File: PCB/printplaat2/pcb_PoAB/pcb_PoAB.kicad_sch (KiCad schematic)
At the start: 30 parts, among them J1 Conn_01x02_Female, J2 INA219_1, J3 INA219_2, J4 INA219_3, J5 INA219_4, J6 lamp1, J7 lamp2, J8 lamp3, U1 L7805CV, U2 AQY211EHAZ, U3 AQY211EHAZ, U4 AQY211EHAZ, U5 ACS712ELCTR-05B-T, U6 ACS712ELCTR-05B-T, U7 ACS712ELCTR-05B-T, U8 ACS712ELCTR-05B-T, U9 ARDUINO_MKR_WAN_1310

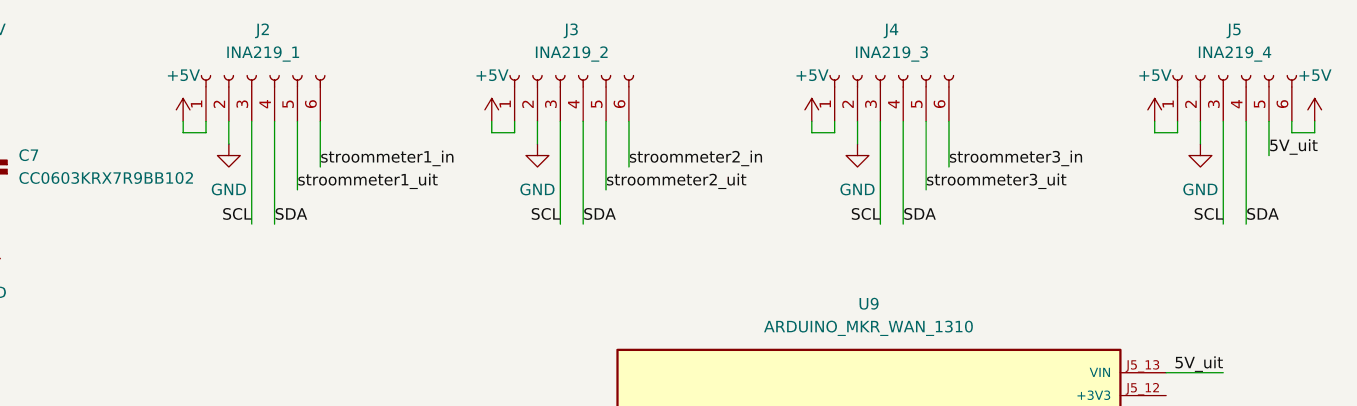
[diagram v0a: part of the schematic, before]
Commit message: pcb lichsensor toegevoegd
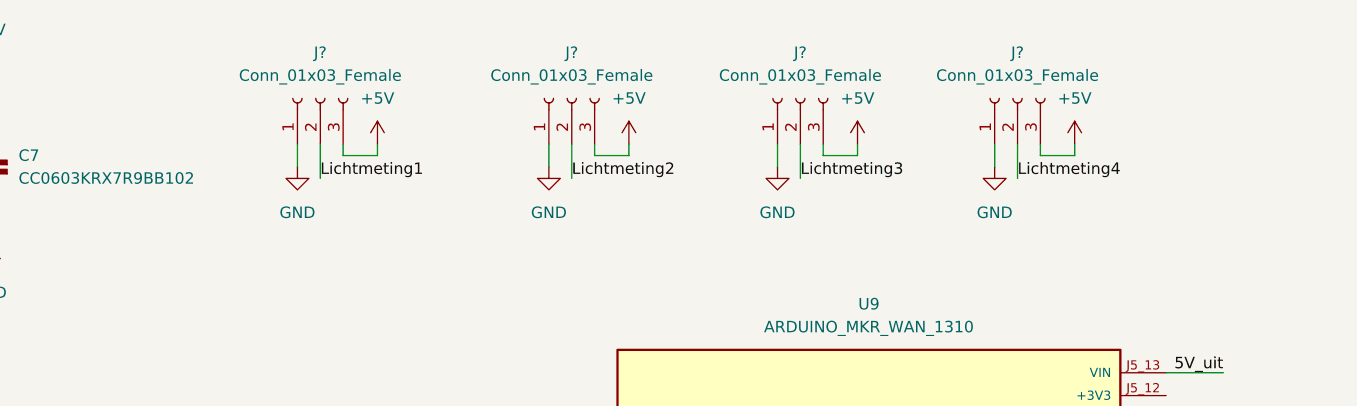
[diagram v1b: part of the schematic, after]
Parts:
- removed J2: INA219_1, symbol Connector:Conn_01x06_Female
- removed J3: INA219_2, symbol Connector:Conn_01x06_Female
- removed J4: INA219_3, symbol Connector:Conn_01x06_Female
- removed J5: INA219_4, symbol Connector:Conn_01x06_Female
- added J? (x4): Conn_01x03_Female, symbol Connector:Conn_01x03_Female
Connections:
- net +5V: now also J?.3 (Pin_3), J?.3 (Pin_3), J?.3 (Pin_3), J?.3 (Pin_3)
- net GND: now also J?.1 (Pin_1), J?.1 (Pin_1), J?.1 (Pin_1), J?.1 (Pin_1)
- new net Lichtmeting1: J?.2 (Pin_2)
- new net Lichtmeting2: J?.2 (Pin_2)
- new net Lichtmeting3: J?.2 (Pin_2)
- new net Lichtmeting4: J?.2 (Pin_2)

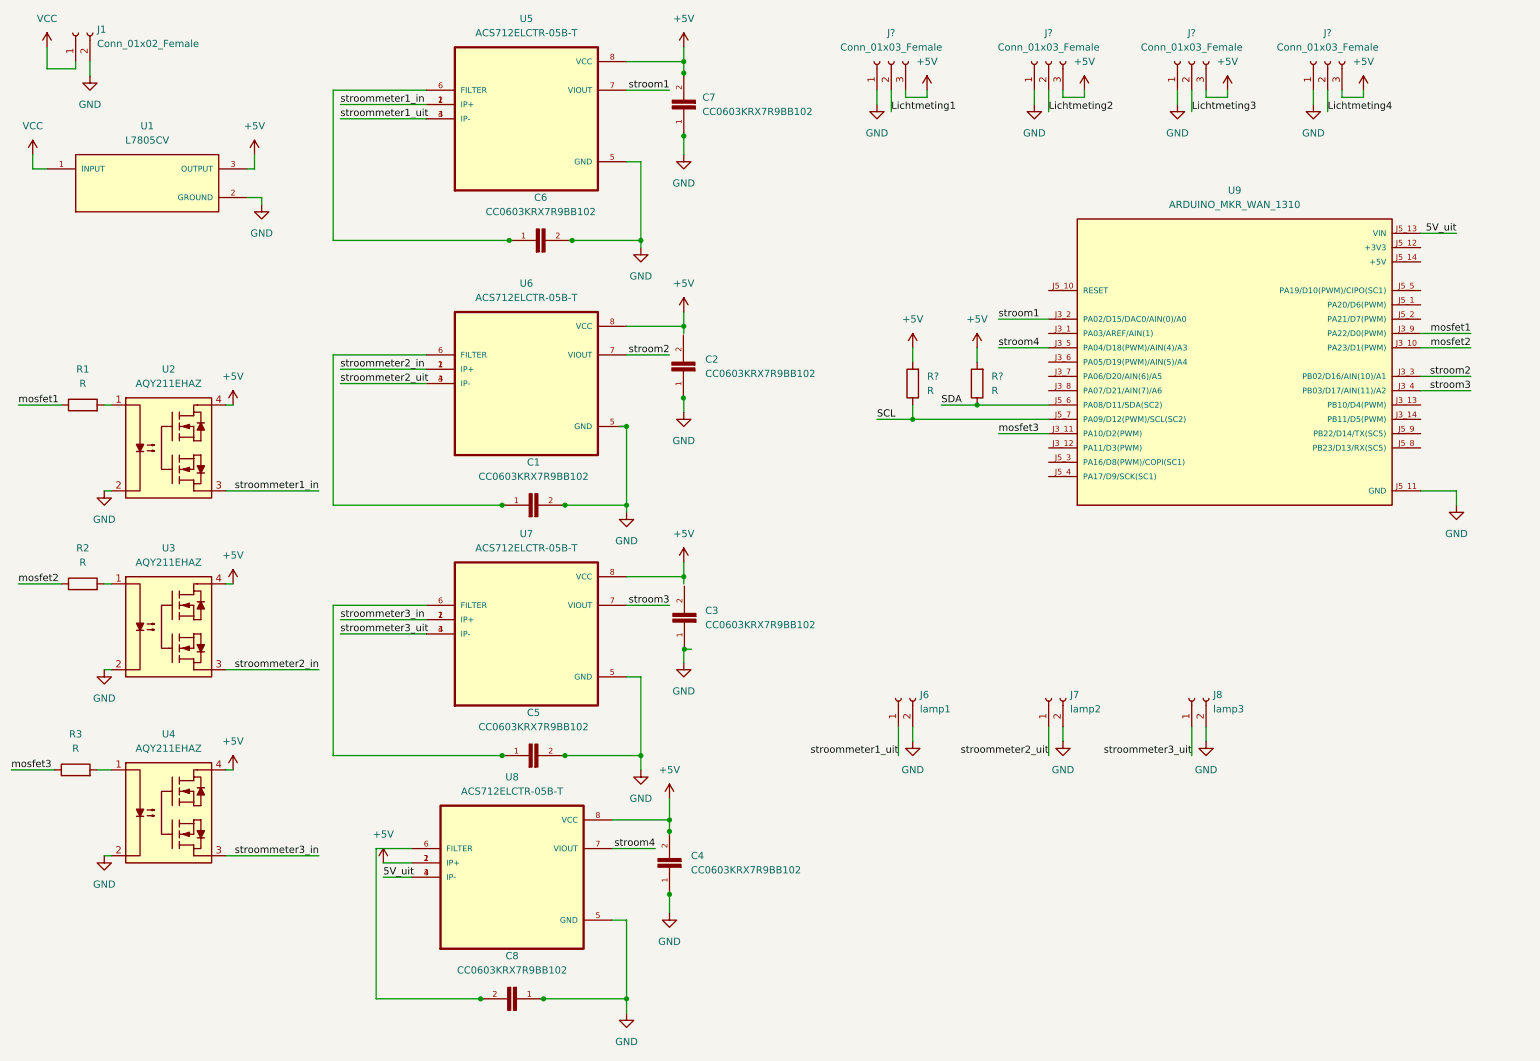
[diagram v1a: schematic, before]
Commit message: lichtmetingen en voltage metingen toegevoegd
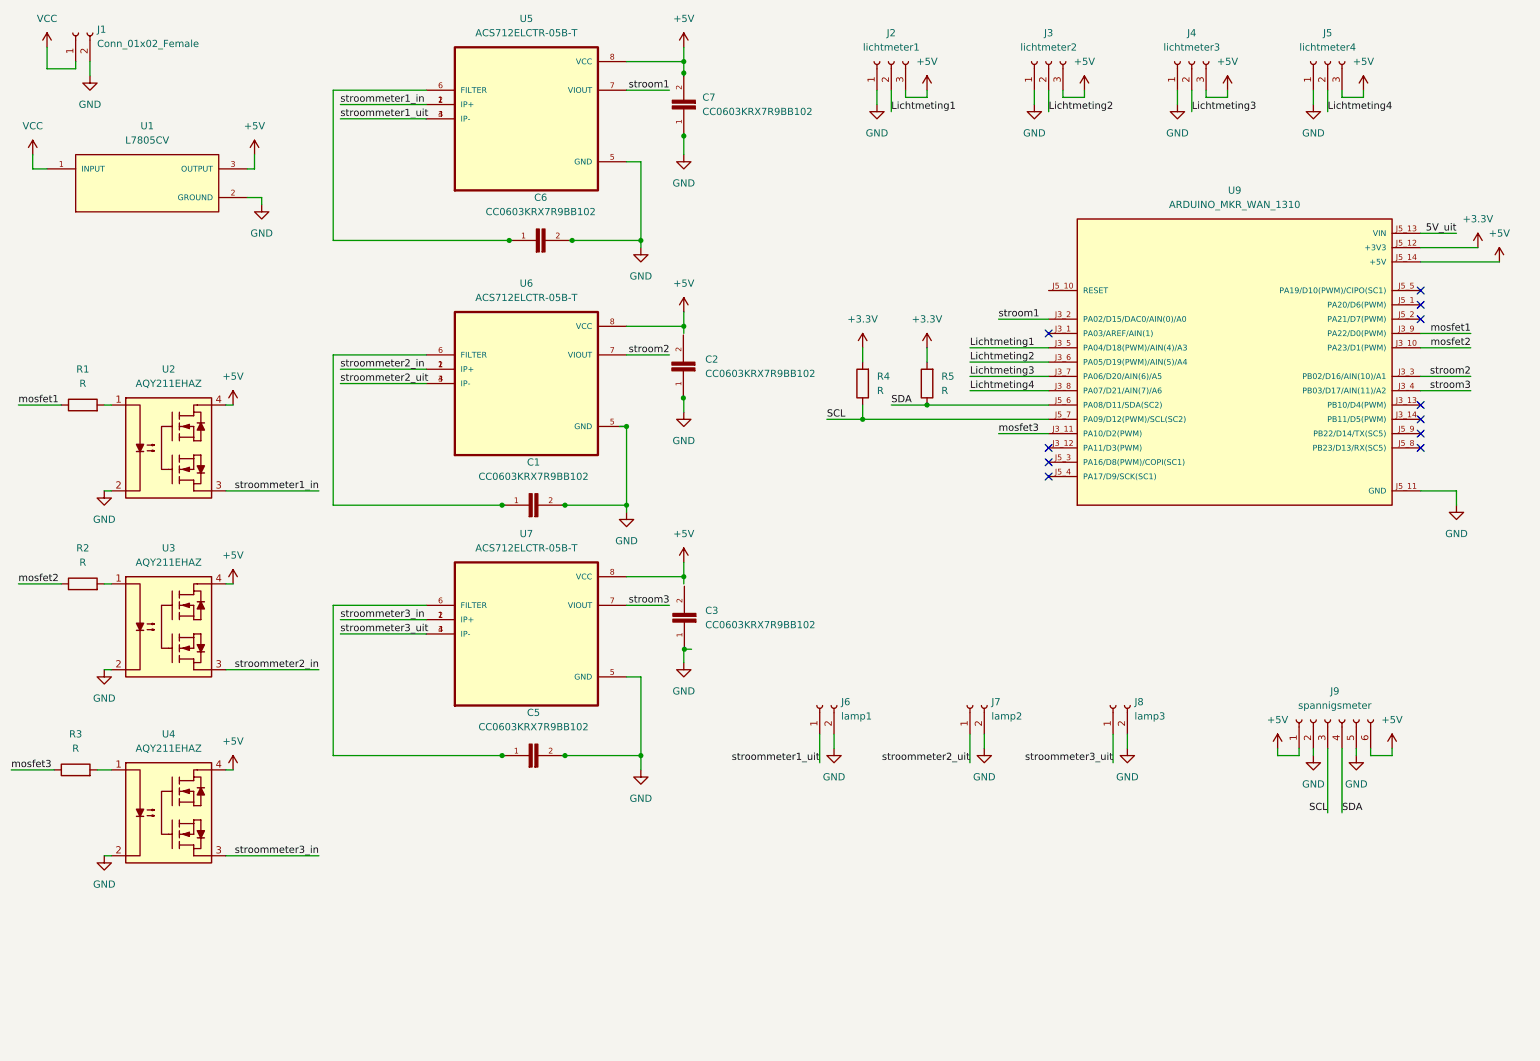
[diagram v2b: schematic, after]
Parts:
- removed C4, C8: CC0603KRX7R9BB102, CAPC1608X90, symbol CC0603KRX7R9BB102:CC0603KRX7R9BB102
- removed U8: ACS712ELCTR-05B-T, SOIC127P600X175-8N, symbol ACS712ELCTR-05B-T:ACS712ELCTR-05B-T
- added J9: spannigsmeter, symbol Connector:Conn_01x06_Female
- J2: renamed from J?; value Conn_01x03_Female -> lichtmeter1
- J3: renamed from J?; value Conn_01x03_Female -> lichtmeter2
- J4: renamed from J?; value Conn_01x03_Female -> lichtmeter3
- J5: renamed from J?; value Conn_01x03_Female -> lichtmeter4
- gave numbers to parts that had none: 2
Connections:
- net stroom4 is gone; now on net Lichtmeting1: U9.J3_5 (PA04/D18(PWM)/AIN(4)/A3)
- net +5V: now also U9.J5_14 (+5V), J9.1 (Pin_1), J9.6 (Pin_6); no longer R4.2, R5.2
- net GND: now also J9.2 (Pin_2), J9.5 (Pin_5)
- net Lichtmeting2: now also U9.J3_6 (PA05/D19(PWM)/AIN(5)/A4)
- net Lichtmeting3: now also U9.J3_7 (PA06/D20/AIN(6)/A5)
- net Lichtmeting4: now also U9.J3_8 (PA07/D21/AIN(7)/A6)
- net SCL: now also J9.3 (Pin_3)
- net SDA: now also J9.4 (Pin_4)
- net +3.3V: now reaches U9.J5_12 (+3V3)
- net +3.3V: now also R4.2, R5.2
- no-connect marks 0 -> 11
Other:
- moved on the sheet: J6, J7, J8, R4, R5

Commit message: spanningsmeter aangepast
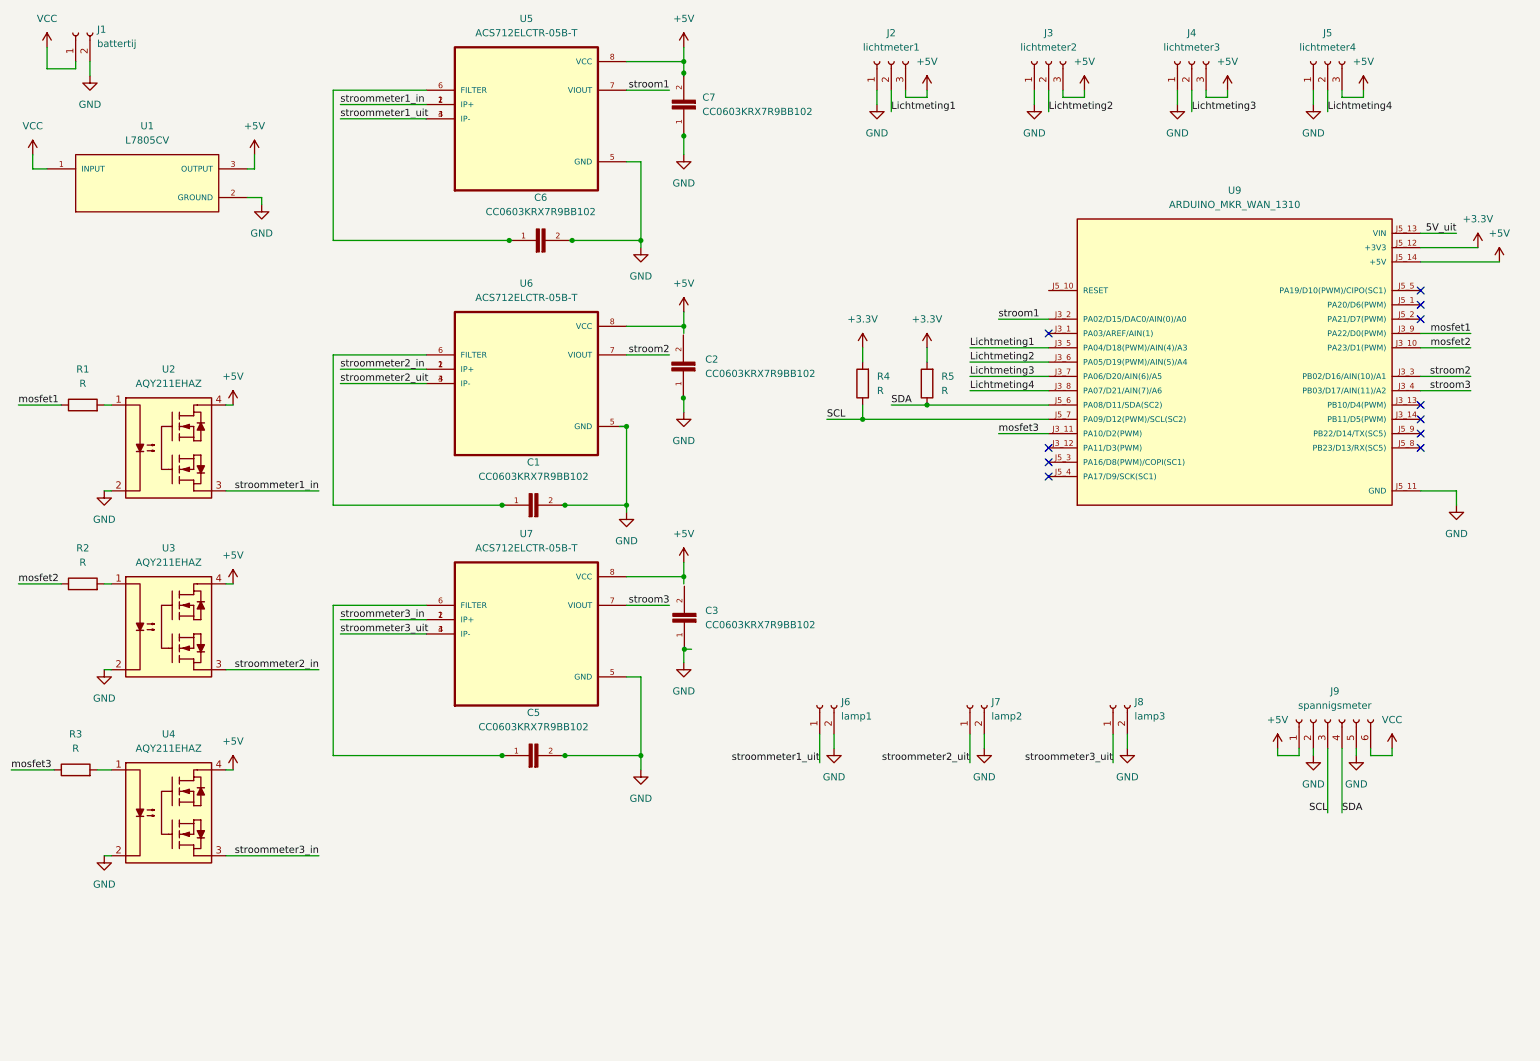
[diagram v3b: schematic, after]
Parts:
- J1: value Conn_01x02_Female -> battertij
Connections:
- net +5V: no longer J9.6 (Pin_6)
- net VCC: now also J9.6 (Pin_6)
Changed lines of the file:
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@@
     (pin "3")
+  )
+  (symbol (lib_id "power:VCC") (at 259.08 143.51 0) (unit 1)
+    (in_bom yes) (on_board yes) (fields_autoplaced)
+    (property "Reference" "#PWR?" (id 0) (at 259.08 147.32 0)
+      (effects (font (size 1.27 1.27)) hide)
+    )
+    (property "Value" "VCC" (id 1) (at 259.08 138.43 0))
+    (property "Footprint" "" (id 2) (at 259.08 143.51 0)
+      (effects (font (size 1.27 1.27)) hide)
+    )
+    (property "Datasheet" "" (id 3) (at 259.08 143.51 0)
+      (effects (font (size 1.27 1.27)) hide)
+    )
+    (pin "1")
   )
   (symbol (lib_id "power:+5V") (at 229.87 26.67 0) (unit 1)
@@
     )
     (property "Datasheet" "" (id 3) (at 58.42 46.99 0)
-      (effects (font (size 1.27 1.27)) hide)
-    )
-    (pin "1")
-  )
-  (symbol (lib_id "power:+5V") (at 259.08 143.51 0) (unit 1)
-    (in_bom yes) (on_board yes) (fields_autoplaced)
-    (property "Reference" "#PWR042" (id 0) (at 259.08 147.32 0)
-      (effects (font (size 1.27 1.27)) hide)
-    )
-    (property "Value" "+5V" (id 1) (at 259.08 138.43 0))
-    (property "Footprint" "" (id 2) (at 259.08 143.51 0)
-      (effects (font (size 1.27 1.27)) hide)
-    )
-    (property "Datasheet" "" (id 3) (at 259.08 143.51 0)
       (effects (font (size 1.27 1.27)) hide)
     )
@@
       (effects (font (size 1.27 1.27)) (justify right))
     )
-    (property "Value" "Conn_01x02_Female" (id 1) (at 29.21 18.4149 90)
+    (property "Value" "battertij" (id 1) (at 29.21 18.4149 90)
       (effects (font (size 1.27 1.27)) (justify right))
     )
@@
       (reference "#PWR041") (unit 1) (value "+5V") (footprint "")
     )
-    (path "/7ac8df71-7403-480d-b51e-8772ef920553"
-      (reference "#PWR042") (unit 1) (value "+5V") (footprint "")
-    )
     (path "/00b7c04c-71c2-4230-b7a8-18f3cfedd146"
       (reference "#PWR?") (unit 1) (value "+3.3V") (footprint "")
@@
       (reference "#PWR?") (unit 1) (value "+3.3V") (footprint "")
     )
+    (path "/69ebda95-083c-43f9-b0df-38d5ed933405"
+      (reference "#PWR?") (unit 1) (value "VCC") (footprint "")
+    )
     (path "/bfeb4a36-78e1-433e-b345-13105a29066a"
       (reference "#PWR?") (unit 1) (value "+5V") (footprint "")
@@
     )
     (path "/bfb5be97-a6a0-4719-bc62-a113d256b0d8"
-      (reference "J1") (unit 1) (value "Conn_01x02_Female") (footprint "")
+      (reference "J1") (unit 1) (value "battertij") (footprint "")
     )
     (path "/8ad6932f-849e-4a86-91ff-fb0687becd73"

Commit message: pcb gemaakt
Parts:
- C1: renamed from C6; footprint CAPC1608X90 -> CC0603KRX7R9BB102:CAPC1608X90
- C2: renamed from C1; footprint CAPC1608X90 -> CC0603KRX7R9BB102:CAPC1608X90
- C3: renamed from C5; footprint CAPC1608X90 -> CC0603KRX7R9BB102:CAPC1608X90
- C4: renamed from C7; footprint CAPC1608X90 -> CC0603KRX7R9BB102:CAPC1608X90
- C5: renamed from C2; footprint CAPC1608X90 -> CC0603KRX7R9BB102:CAPC1608X90
- C6: renamed from C3; footprint CAPC1608X90 -> CC0603KRX7R9BB102:CAPC1608X90
- J1, J6, J7, J8: footprint (none) -> Connector_PinSocket_2.54mm:PinSocket_1x02_P2.54mm_Vertical
- J2, J3, J4, J5: footprint (none) -> Connector_PinSocket_2.54mm:PinSocket_1x03_P2.54mm_Vertical
- J9: footprint (none) -> Connector_PinSocket_2.54mm:PinSocket_1x06_P2.54mm_Vertical
- R1, R2, R3, R4, R5: footprint (none) -> Resistor_SMD:R_0805_2012Metric_Pad1.20x1.40mm_HandSolder
- U1: footprint TO255P1040X460X1968-3 -> L7805CV:TO255P1040X460X1968-3
- U2, U3, U4: footprint (none) -> PoAB_Foots2:AQY211EHAZ
- U5, U6, U7: footprint SOIC127P600X175-8N -> ACS712ELCTR-05B-T:SOIC127P600X175-8N
- U9: footprint BOARD_ARDUINO_MKR_WAN_1310 -> ARDUINO_MKR_WAN_1310:BOARD_ARDUINO_MKR_WAN_1310
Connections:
- net 5V_uit is gone; now on net +5V: U9.J5_13 (VIN)
- net +5V: now also C5.2, C6.2
- net GND: now also C5.1, C6.1
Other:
- moved on the sheet: C5

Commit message: spannings meting en bord spanning aangepast pcb en schema
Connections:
- net +5V: no longer C4.2, C5.2, C6.2, J2.3 (Pin_3), J3.3 (Pin_3), J4.3 (Pin_3), J5.3 (Pin_3), J9.1 (Pin_1), U2.4 (VCC), U3.4 (VCC), U4.4 (VCC), U5.8 (VCC), U6.8 (VCC), U7.8 (VCC), U9.J5_14 (+5V)
- net GND: no longer J9.5 (Pin_5)
- net VCC: no longer U1.1 (INPUT)
- new net 5V_bord: C4.2, C5.2, C6.2, J2.3 (Pin_3), J3.3 (Pin_3), J4.3 (Pin_3), J5.3 (Pin_3), J9.1 (Pin_1), U2.4 (VCC), U3.4 (VCC), U4.4 (VCC), U5.8 (VCC), U6.8 (VCC), U7.8 (VCC), U9.J5_14 (+5V)
- new net regelaar_in: J9.5 (Pin_5), U1.1 (INPUT)
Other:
- moved on the sheet: U1
